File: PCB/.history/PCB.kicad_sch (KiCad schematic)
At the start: 20 parts, among them J1 USB_C_Receptacle_USB2.0_14P, J2 OLED_128x64, SW1 SW_Push, U1 STM32F072CBTx, U2 USBLC6-2SC6, U3 XC6206, U5 TRRS

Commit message: Started trying to route the traces
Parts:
- C1, C2, C3, C4, C5, C6, C7: footprint (none) -> Capacitor_SMD:C_0805_2012Metric
- C8, C9: value 1 uF -> 1uF; footprint (none) -> Capacitor_SMD:C_0805_2012Metric
- F1: footprint (none) -> Fuse:Fuse_0805_2012Metric
- J1: footprint (none) -> Connector_USB:USB_C_Receptacle_HRO_TYPE-C-31-M-12
- J2: footprint ScottoKeebs_Components:OLED_128x64 -> Connector_PinHeader_2.54mm:PinHeader_1x04_P2.54mm_Vertical
- R1: renamed from 5.1k1; value Resistor -> 5.1k; footprint (none) -> Resistor_SMD:R_0805_2012Metric
- R2: renamed from 5.1k2; value Resistor -> 5.1k; footprint (none) -> Resistor_SMD:R_0805_2012Metric
- R3: renamed from 10k1; value Resistor -> 10k; footprint (none) -> Resistor_SMD:R_0805_2012Metric
- SW1: footprint (none) -> Button_Switch_SMD:SW_SPST_TL3342
- U5: footprint ScottoKeebs_Components:TRRS_PJ-320A -> Connector_Audio:Jack_3.5mm_PJ311_Horizontal
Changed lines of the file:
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@@
 		)
 		(property "Value" "100nF"
-			(at 53.594 169.418 90)
+			(at 58.928 160.274 0)
 			(show_name no)
 			(do_not_autoplace no)
@@
 					(size 1.27 1.27)
 				)
-				(justify left)
+				(justify right)
 			)
 		)
-		(property "Footprint" ""
+		(property "Footprint" "Capacitor_SMD:C_0805_2012Metric"
 			(at 58.1152 170.18 0)
 			(hide yes)
@@
 		(in_pos_files yes)
 		(dnp no)
-		(property "Reference" "5.1k1"
+		(property "Reference" "R1"
 			(at 224.79 44.45 0)
 			(show_name no)
@@
 			)
 		)
-		(property "Value" "Resistor"
+		(property "Value" "5.1k"
 			(at 224.536 42.418 0)
 			(show_name no)
@@
 			)
 		)
-		(property "Footprint" ""
+		(property "Footprint" "Resistor_SMD:R_0805_2012Metric"
 			(at 224.79 46.228 0)
 			(hide yes)
@@
 			(project "PCB"
 				(path "/61897acb-2078-4c47-92ce-82a0439bac7e"
-					(reference "5.1k1")
+					(reference "R1")
 					(unit 1)
 				)
@@
 			)
 		)
-		(property "Footprint" "ScottoKeebs_Components:TRRS_PJ-320A"
+		(property "Footprint" "Connector_Audio:Jack_3.5mm_PJ311_Horizontal"
 			(at 154.94 81.28 0)
 			(hide yes)
@@
 		)
 		(property "Value" "100nF"
-			(at 43.434 169.418 90)
+			(at 48.514 160.528 0)
 			(show_name no)
 			(do_not_autoplace no)
@@
 					(size 1.27 1.27)
 				)
-				(justify left)
+				(justify right)
 			)
 		)
-		(property "Footprint" ""
+		(property "Footprint" "Capacitor_SMD:C_0805_2012Metric"
 			(at 47.9552 170.18 0)
 			(hide yes)
@@
 		)
 		(property "Value" "10nF"
-			(at 73.914 169.418 90)
+			(at 74.676 161.036 0)
 			(show_name no)
 			(do_not_autoplace no)
@@
 			)
 		)
-		(property "Footprint" ""
+		(property "Footprint" "Capacitor_SMD:C_0805_2012Metric"
 			(at 78.4352 170.18 0)
 			(hide yes)
@@
 		)
 		(property "Value" "100nF"
-			(at 23.114 169.418 90)
+			(at 22.606 168.148 90)
 			(show_name no)
 			(do_not_autoplace no)
@@
 			)
 		)
-		(property "Footprint" ""
+		(property "Footprint" "Capacitor_SMD:C_0805_2012Metric"
 			(at 27.6352 170.18 0)
 			(hide yes)
@@
 			)
 		)
-		(property "Footprint" ""
+		(property "Footprint" "Fuse:Fuse_0805_2012Metric"
 			(at 229.87 41.148 0)
 			(hide yes)
@@
 			)
 		)
-		(property "Value" "1 uF"
+		(property "Value" "1uF"
 			(at 254 40.6399 0)
 			(show_name no)
@@
 			)
 		)
-		(property "Footprint" ""
+		(property "Footprint" "Capacitor_SMD:C_0805_2012Metric"
 			(at 251.1552 43.18 0)
 			(hide yes)
@@
 		)
 		(property "Value" "100nF"
-			(at 33.274 169.418 90)
+			(at 38.862 160.274 0)
 			(show_name no)
 			(do_not_autoplace no)
@@
 					(size 1.27 1.27)
 				)
-				(justify left)
+				(justify right)
 			)
 		)
-		(property "Footprint" ""
+		(property "Footprint" "Capacitor_SMD:C_0805_2012Metric"
 			(at 37.7952 170.18 0)
 			(hide yes)
@@
 		(in_pos_files yes)
 		(dnp no)
-		(property "Reference" "5.1k2"
+		(property "Reference" "R2"
 			(at 224.79 46.99 0)
 			(show_name no)
@@
 			)
 		)
-		(property "Value" "Resistor"
+		(property "Value" "5.1k"
 			(at 225.298 49.276 0)
 			(show_name no)
@@
 			)
 		)
-		(property "Footprint" ""
+		(property "Footprint" "Resistor_SMD:R_0805_2012Metric"
 			(at 224.79 48.768 0)
 			(hide yes)
@@
 			(project "PCB"
 				(path "/61897acb-2078-4c47-92ce-82a0439bac7e"
-					(reference "5.1k2")
+					(reference "R2")
 					(unit 1)
 				)
@@
 			)
 		)
-		(property "Footprint" "ScottoKeebs_Components:OLED_128x64"
+		(property "Footprint" "Connector_PinHeader_2.54mm:PinHeader_1x04_P2.54mm_Vertical"
 			(at 92.71 82.55 0)
 			(hide yes)
@@
 			)
 		)
-		(property "Footprint" ""
+		(property "Footprint" "Connector_USB:USB_C_Receptacle_HRO_TYPE-C-31-M-12"
 			(at 208.28 54.61 0)
 			(hide yes)
@@
 			)
 		)
-		(property "Footprint" ""
+		(property "Footprint" "Button_Switch_SMD:SW_SPST_TL3342"
 			(at 91.44 97.79 0)
 			(hide yes)
@@
 			)
 		)
-		(property "Footprint" ""
+		(property "Footprint" "Capacitor_SMD:C_0805_2012Metric"
 			(at 30.48 63.8048 0)
 			(hide yes)
@@
 		(in_pos_files yes)
 		(dnp no)
-		(fields_autoplaced yes)
-		(property "Reference" "10k1"
-			(at 104.14 96.52 0)
+		(property "Reference" "R3"
+			(at 104.14 102.87 0)
 			(show_name no)
 			(do_not_autoplace no)
@@
 			)
 		)
-		(property "Value" "Resistor"
-			(at 104.14 99.06 0)
+		(property "Value" "10k"
+			(at 103.886 100.33 0)
 			(show_name no)
 			(do_not_autoplace no)
@@
 			)
 		)
-		(property "Footprint" ""
+		(property "Footprint" "Resistor_SMD:R_0805_2012Metric"
 			(at 104.14 104.648 0)
 			(hide yes)
@@
 			(project "PCB"
 				(path "/61897acb-2078-4c47-92ce-82a0439bac7e"
-					(reference "10k1")
+					(reference "R3")
 					(unit 1)
 				)
@@
 			)
 		)
-		(property "Value" "1 uF"
+		(property "Value" "1uF"
 			(at 275.59 40.6399 0)
 			(show_name no)
@@
 			)
 		)
-		(property "Footprint" ""
+		(property "Footprint" "Capacitor_SMD:C_0805_2012Metric"
 			(at 272.7452 43.18 0)
 			(hide yes)
@@
 		)
 		(property "Value" "100nF"
-			(at 63.754 169.418 90)
+			(at 65.024 161.036 0)
 			(show_name no)
 			(do_not_autoplace no)
@@
 			)
 		)
-		(property "Footprint" ""
+		(property "Footprint" "Capacitor_SMD:C_0805_2012Metric"
 			(at 68.2752 170.18 0)
 			(hide yes)

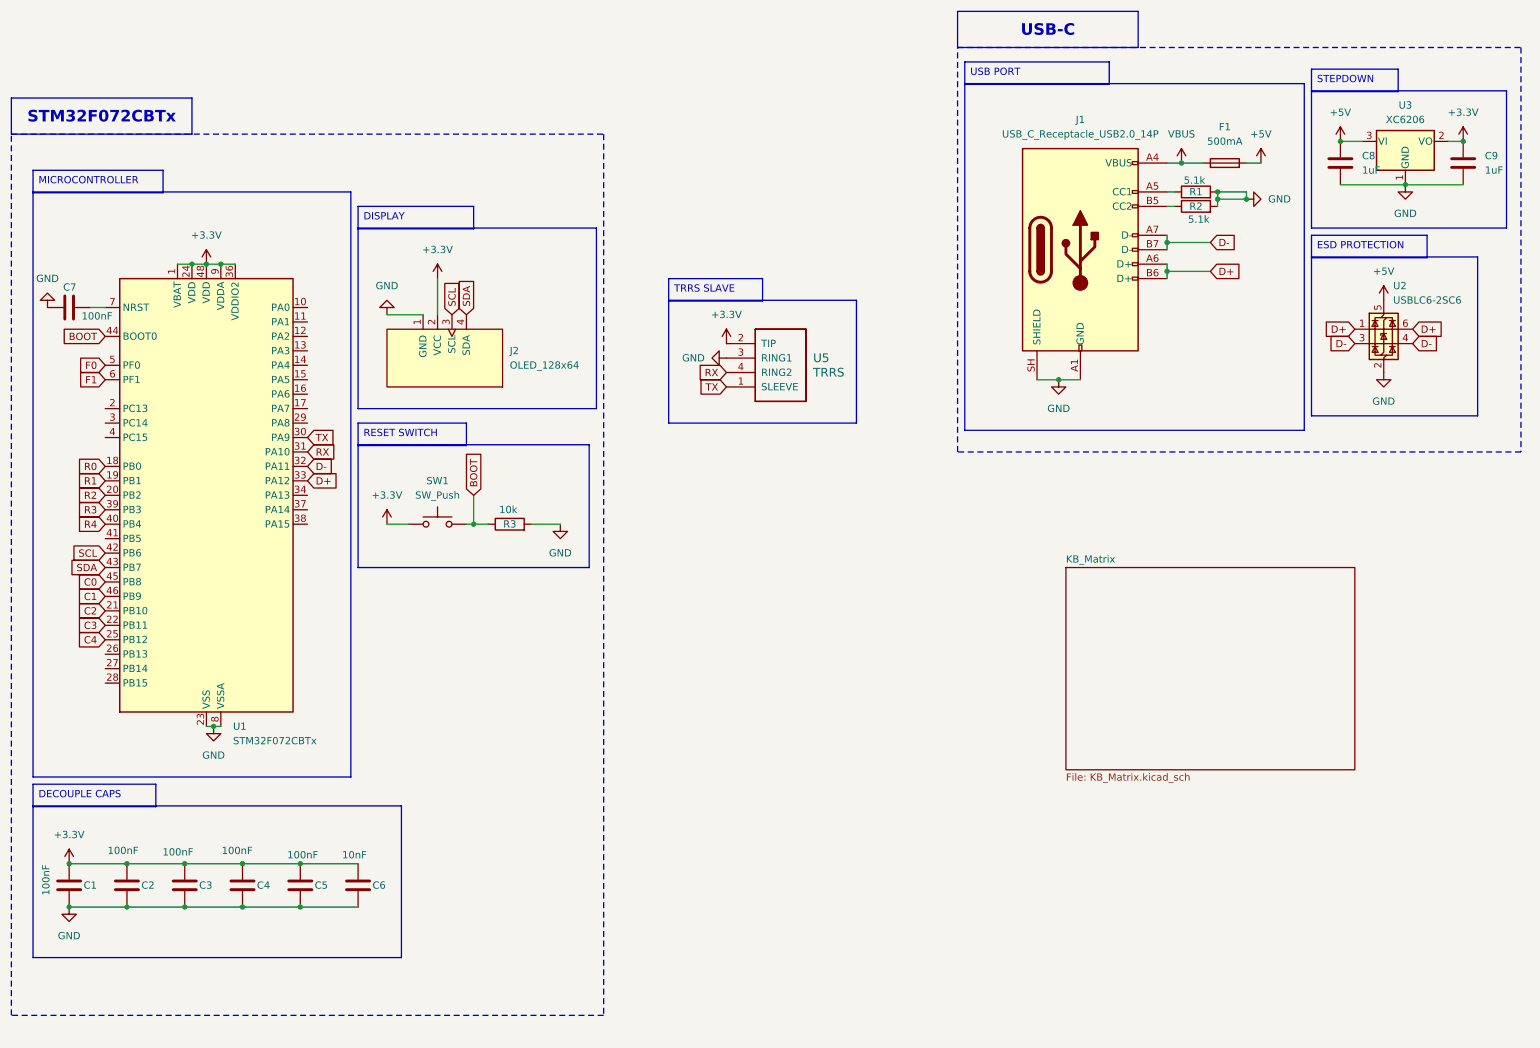
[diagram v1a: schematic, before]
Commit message: Added rotatry knobs to sketch
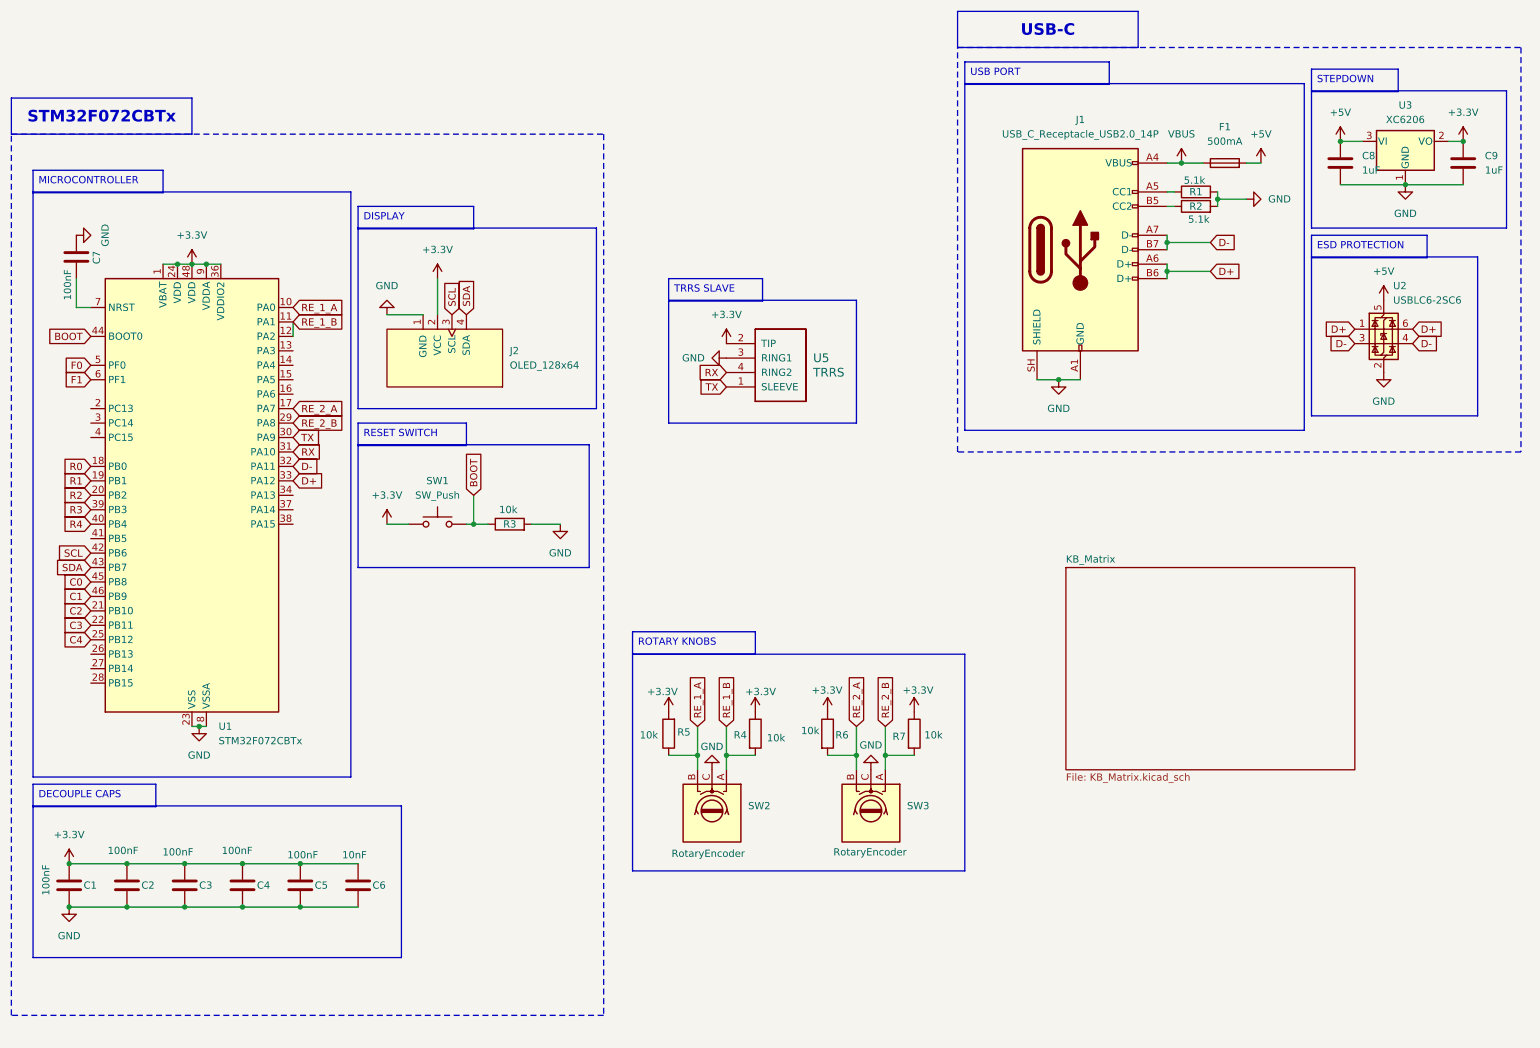
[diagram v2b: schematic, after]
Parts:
- added R4, R5, R6, R7: 10k, Resistor_SMD:R_0805_2012Metric, symbol ScottoKeebs:Placeholder_Resistor
- added SW2, SW3: RotaryEncoder, Rotary_Encoder:RotaryEncoder_Alps_EC11E_Vertical_H20mm, symbol Device:RotaryEncoder
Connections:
- net +3.3V: now also R4.1, R5.2, R6.1, R7.1
- net GND: now also SW2.C, SW3.C
- net RE_1_A: now reaches U1.10 (PA0)
- net RE_1_A: now also R5.1, SW2.B
- net RE_1_B: now reaches U1.11 (PA1)
- net RE_1_B: now also U1.12 (PA2), R4.2, SW2.A
- net RE_2_A: now reaches U1.17 (PA7)
- net RE_2_A: now also R6.2, SW3.B
- net RE_2_B: now reaches U1.29 (PA8)
- net RE_2_B: now also R7.2, SW3.A
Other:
- moved on the sheet: C7, U1

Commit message: Improved routing and the first final iteration of PCB
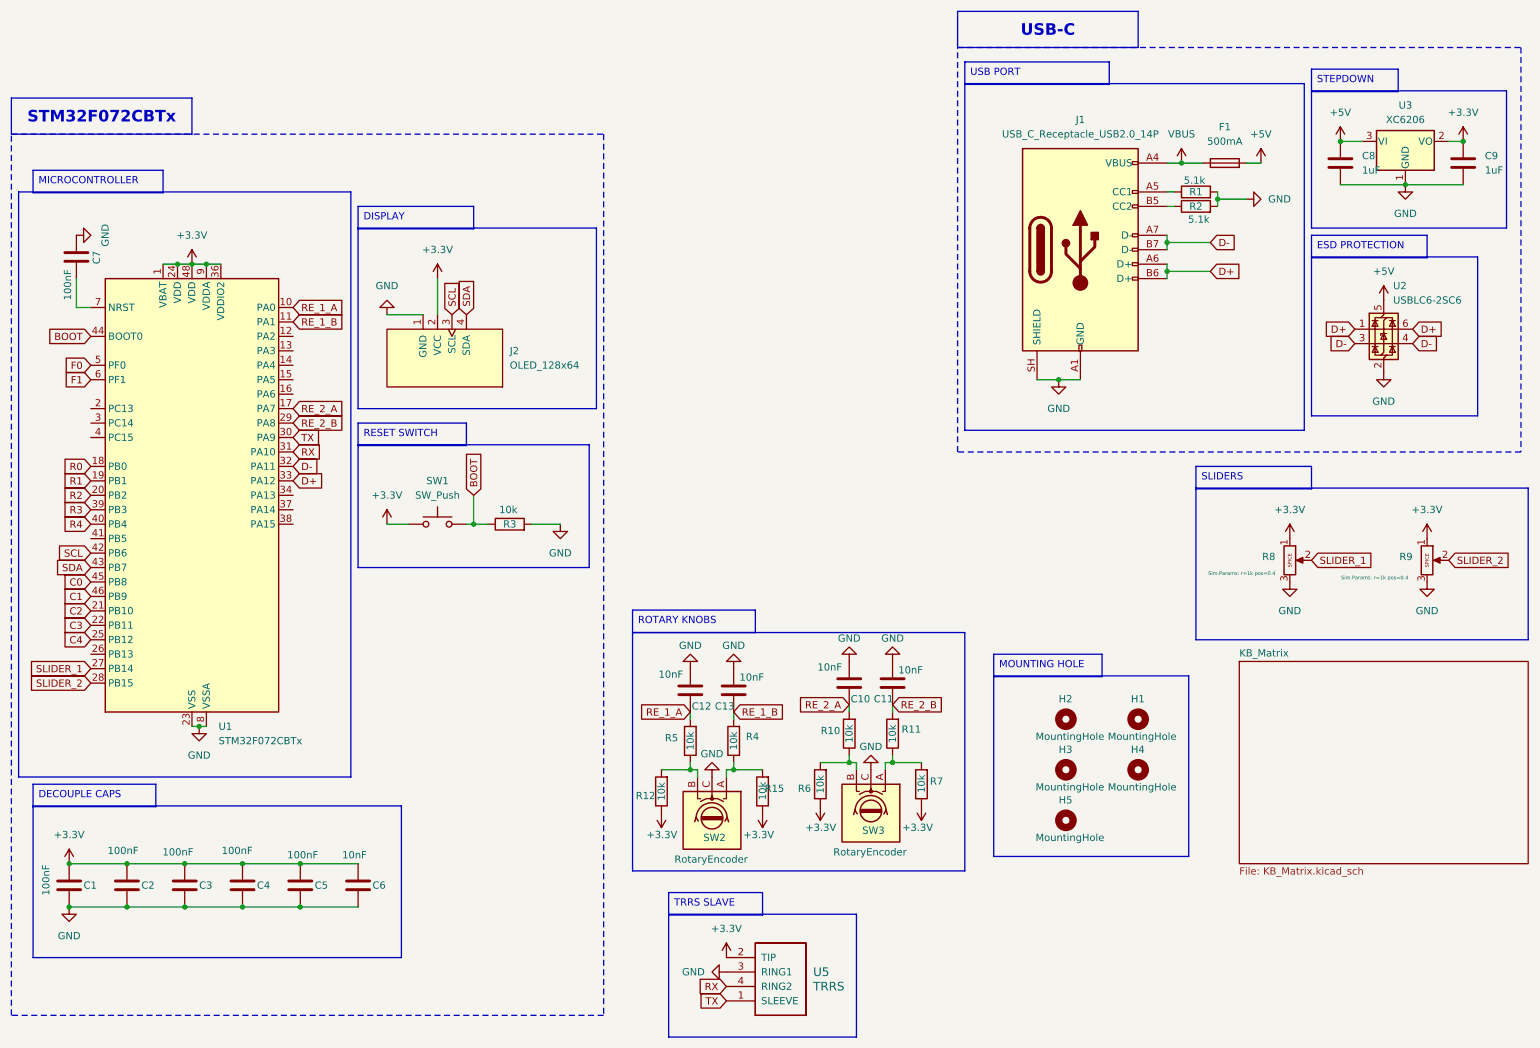
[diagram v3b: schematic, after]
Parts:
- added C10, C11, C12, C13: 10nF, Capacitor_SMD:C_0805_2012Metric, symbol Device:C
- added H1, H2, H3, H4, H5: MountingHole, MountingHole:MountingHole_2.7mm, symbol Mechanical:MountingHole
- added R10, R11, R12, R15: 10k, Resistor_SMD:R_0805_2012Metric, symbol ScottoKeebs:Placeholder_Resistor
- added R8, R9: Potentiometer, Potentiometer_THT:Potentiometer_Bourns_PTA6043_Single_Slide, symbol Simulation_SPICE:Potentiometer
- SW2, SW3: footprint Rotary_Encoder:RotaryEncoder_Alps_EC11E_Vertical_H20mm -> Rotary_Encoder:RotaryEncoder_Alps_EC12E-Switch_Vertical_H20mm
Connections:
- net +3.3V: now also R12.1, R15.1, R8.1, R9.1; no longer R4.1, R5.2
- net GND: now also C10.1, C11.1, C12.1, C13.1, R8.3, R9.3
- net RE_1_A: now also R5.2, C12.2; no longer R5.1, SW2.B
- net RE_1_B: now also C13.2; no longer SW2.A, U1.12 (PA2)
- net RE_2_A: now also C10.2, R10.2; no longer R6.2, SW3.B
- net RE_2_B: now also C11.2, R11.2; no longer R7.2, SW3.A
- net SLIDER_1: now reaches U1.27 (PB14)
- net SLIDER_1: now also R8.2
- net SLIDER_2: now reaches U1.28 (PB15)
- net SLIDER_2: now also R9.2
- new net: R15.2, R4.1, SW2.A
- new net: R12.2, R5.1, SW2.B
- new net: R10.1, R6.2, SW3.B
- new net: R11.1, R7.2, SW3.A
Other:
- moved on the sheet: R6, R7, U5

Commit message: Updated
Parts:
- added J3: Micro_SD_Card_Det1, symbol Connector:Micro_SD_Card_Det1
- added R13, R14, R16: 10k, symbol Device:R
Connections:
- net +3.3V: now also J3.4 (VDD), R13.1, R14.1, R16.1
- net GND: now also J3.6 (VSS), J3.SH (SHIELD)
- net SLIDER_1: now also U1.13 (PA3); no longer U1.27 (PB14)
- net SLIDER_2: now also U1.12 (PA2); no longer U1.28 (PB15)
- net CS: now reaches U1.14 (PA4)
- net CS: now also J3.2 (DAT3/CD), R14.2
- net IS_SD: now reaches U1.15 (PA5)
- net IS_SD: now also J3.9 (DET)
- net SCK: now reaches U1.26 (PB13)
- net SCK: now also J3.5 (CLK)
- new net MISO: J3.7 (DAT0), R16.2, U1.27 (PB14)
- new net MOSI: J3.3 (CMD), R13.2, U1.28 (PB15)
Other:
- moved on the sheet: C7, H1, H2, H3, H4, H5, U1

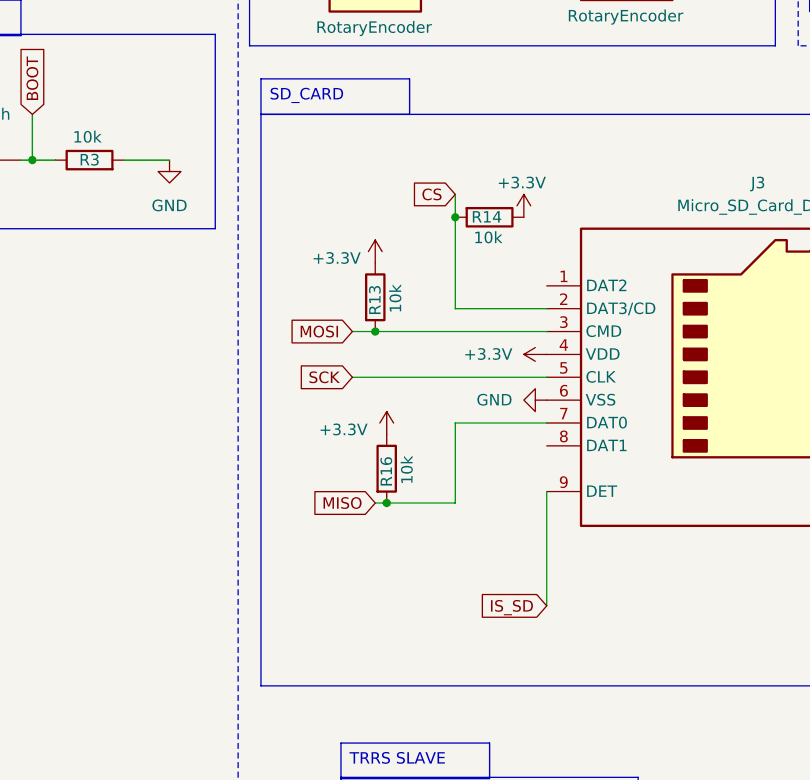
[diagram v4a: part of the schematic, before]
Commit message: Added sd card and fixed some wirings
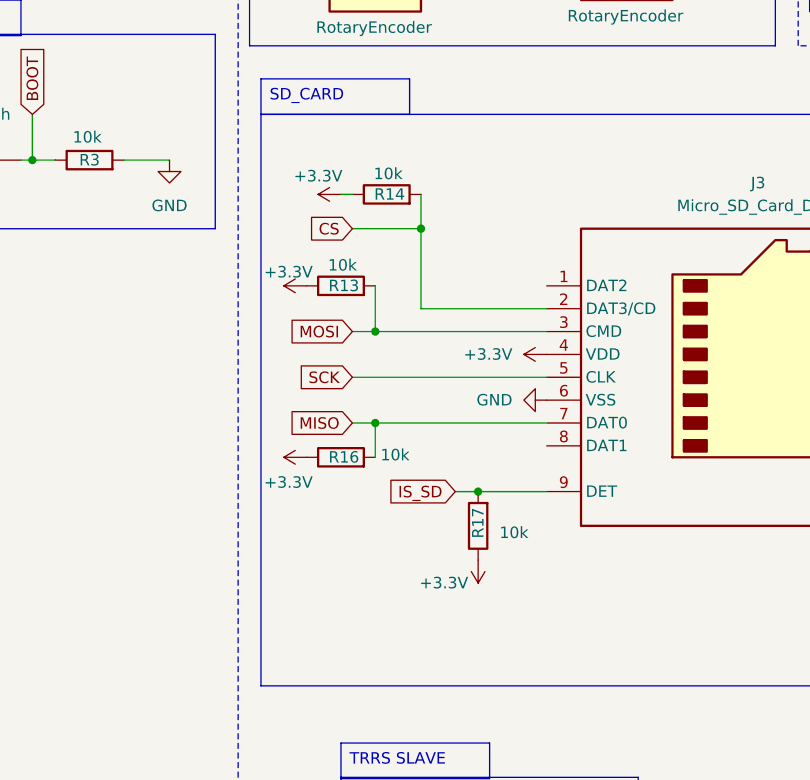
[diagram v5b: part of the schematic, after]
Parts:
- added R17: 10k, Resistor_SMD:R_0805_2012Metric, symbol Device:R
- J3: footprint (none) -> Connector_Card:microSD_HC_Hirose_DM3AT-SF-PEJM5
- R13, R14, R16: footprint (none) -> Resistor_SMD:R_0805_2012Metric
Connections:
- net +3.3V: now also R17.1
- net IS_SD: now also R17.2
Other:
- moved on the sheet: R13, R14, R16
